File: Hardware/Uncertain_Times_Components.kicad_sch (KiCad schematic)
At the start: 73 parts, among them J1 Conn_01x12_Male, J2 Conn_01x16_Male, J3 Conn_01x14_Male, J4 Conn_01x12_Male, J5 SWD_Header, J6 Eurorack_10_pin_power, Q1 MMBT3904, Q2 MMBT3904, U1 LM1117-3.3, U2 STM32G473V, U3 LM1117-5.0, U4 TL074, U6 TL074, Y1 8MHz 20pF

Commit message: Schematic Updates
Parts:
- removed J6: Eurorack_10_pin_power, Custom_Footprints:Eurorack_10_pin_header, symbol Eurorack Header:Eurorack_10_pin_power
- added J7: Eurorack_16_pin_power, Custom_Footprints:Eurorack_16_pin_header, symbol Eurorack Header:Eurorack_16_pin_power
- added R1, R11, R12, R20, R24, R25: 560, Resistor_SMD:R_0603_1608Metric, symbol Device:R
- added R26: 15k, Resistor_SMD:R_0603_1608Metric, symbol Device:R_Small
- added R27: 10k, Resistor_SMD:R_0603_1608Metric, symbol Device:R_Small
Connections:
- net EnvA1_LED_Out is gone; now on net Sine3_Ramp_Lvl_LED: R80.1
- net EnvA2_LED_Out is gone; now on net Sine1_Swell_Lvl_LED: R81.1
- net EnvA3_LED_Out is gone; now on net Sine2_Swell_Lvl_LED: R82.1
- net EnvA4_LED_Out is gone; now on net Sine3_Swell_Lvl_LED: R83.1
- net EnvB1_LED_Out is gone; now on net Ramp_LED: R76.1
- net EnvB2_LED_Out is gone; now on net Swell_LED: R77.1
- net EnvB3_LED_Out is gone; now on net Sine1_Ramp_Lvl_LED: R78.1
- net EnvB4_LED_Out is gone; now on net Sine2_Ramp_Lvl_LED: R79.1
- net +12V_IN: now also J7.10 (Pin_10), J7.9 (Pin_9)
- net -12V_IN: now also J7.1 (Pin_1), J7.2 (Pin_2)
- net FM2_Out: now also J2.5 (Pin_5); no longer J2.7 (Pin_7)
- net FM3_Out: now also J2.6 (Pin_6); no longer J2.10 (Pin_10)
- net GND: now also J7.3 (Pin_3), J7.4 (Pin_4), J7.5 (Pin_5), J7.6 (Pin_6), J7.7 (Pin_7), J7.8 (Pin_8)
- net Sine1_DAC: now also R27.2
- net Sine1_Out: now also J2.2 (Pin_2)
- net Sine2_Out: now also J2.3 (Pin_3)
- net Sine3_Out: now also J2.4 (Pin_4)
- net Swell_Out: now also J2.7 (Pin_7); no longer J2.4 (Pin_4)
- net TIM2_CH3: now also R24.2
- net TIM2_CH4: now also R25.2
- net TIM4_CH1: now also R80.2
- net TIM4_CH2: now also R81.2
- net TIM4_CH3: now also R82.2
- net TIM4_CH4: now also R83.2
- net TIM8_CH1: now also R1.2
- net TIM8_CH2: now also R11.2
- net TIM8_CH3: now also R12.2
- net TIM8_CH4: now also R20.2
- net Sine1_Inv_Out: now reaches J2.8 (Pin_8)
- net Sine1_Inv_Out: now also U6.1, R26.1
- net Sine1_Ramp_Lvl_LED: now reaches J1.10 (Pin_10)
- net Sine2_Ramp_Rate_LED: now reaches J1.11 (Pin_11)
- net Sine2_Ramp_Rate_LED: now also R11.1
- net Sine2_Ramp_Lvl_LED: now reaches J1.12 (Pin_12)
- net Ramp_LED: now reaches J1.7 (Pin_7)
- net Swell_LED: now reaches J1.8 (Pin_8)
- net Sine1_Ramp_Rate_LED: now reaches J1.9 (Pin_9)
- net Sine1_Ramp_Rate_LED: now also R1.1
- net Gate_Normal: now reaches J3.1 (Pin_1)
- net Gate_Normal: now also J7.16 (Pin_16)
- net Sine3_Ramp_Rate_LED: now reaches J3.2 (Pin_2)
- net Sine3_Ramp_Rate_LED: now also R12.1
- net Sine3_Ramp_Lvl_LED: now reaches J3.3 (Pin_3)
- net Sine1_Swell_Rate_LED: now reaches J3.4 (Pin_4)
- net Sine1_Swell_Rate_LED: now also R20.1
- net Sine1_Swell_Lvl_LED: now reaches J3.5 (Pin_5)
- net Sine2_Swell_Rate_LED: now reaches J3.6 (Pin_6)
- net Sine2_Swell_Rate_LED: now also R24.1
- net Sine2_Swell_Lvl_LED: now reaches J3.7 (Pin_7)
- net Sine3_Swell_Rate_LED: now reaches J3.8 (Pin_8)
- net Sine3_Swell_Rate_LED: now also R25.1
- net Sine3_Swell_Lvl_LED: now reaches J3.9 (Pin_9)
- net at U6.2 (-): now also R26.2, R27.1; no longer U6.1
- no-connect marks 27 -> 31
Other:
- moved on the sheet: C21, C22, J3, U4E, U6A, U6E

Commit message: First draft of schematic
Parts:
- removed C17: 10uF, Capacitor_SMD:C_1206_3216Metric, symbol Device:C
- removed C20: 22uF, Capacitor_SMD:CP_Elec_4x5.8, symbol Device:C
- removed FID1: Fiducial, Custom_Footprints:4_Layer_Markers, symbol Mechanical:Fiducial
- removed J2: Conn_01x16_Male, Connector_PinHeader_2.54mm:PinHeader_1x16_P2.54mm_Vertical, symbol Connector:Conn_01x16_Male
- removed J3: Conn_01x14_Male, Connector_PinHeader_2.54mm:PinHeader_1x14_P2.54mm_Vertical, symbol Connector:Conn_01x14_Male
- removed TP6: TestPoint, Custom_Footprints:1mm_Test_Point, symbol Connector:TestPoint
- removed U1: LM1117-3.3, Package_TO_SOT_SMD:SOT-223-3_TabPin2, symbol Regulator_Linear:LM1117-3.3
- removed U3: LM1117-5.0, Package_TO_SOT_SMD:SOT-223-3_TabPin2, symbol Regulator_Linear:LM1117-5.0
- added J2: Conn_01x10_Male, Connector_PinHeader_2.54mm:PinHeader_1x10_P2.54mm_Vertical, symbol Connector:Conn_01x12_Pin
- added J3: Conn_01x12_Male, Connector_PinHeader_2.54mm:PinHeader_1x12_P2.54mm_Vertical, symbol Connector:Conn_01x16_Pin
- added J7: UART_Test_Pins, Custom_Footprints:SWD_header, symbol Connector:Conn_01x02_Pin
- added J8: USB_B_Micro, Custom_Footprints:USB_Micro-B_Amphenol, symbol Connector:USB_B_Micro
- added R34, R35, R36: 560, Resistor_SMD:R_0603_1608Metric, symbol Device:R
- added U2: STF202-22T1G, Custom_Footprints:STF202-22T1G, symbol STF202-22T1G:STF202-22T1G
- added U5: LT1117-3.3, Package_TO_SOT_SMD:SOT-223-3_TabPin2, symbol Regulator_Linear:LT1117-3.3
- C10: renamed from C11; symbol Encoder:CP_Small -> Device:C_Polarized_Small
- C11: renamed from C12; symbol Encoder:CP_Small -> Device:C_Polarized_Small
- C14: renamed from C6; symbol Encoder:CP_Small -> Device:C_Polarized_Small
- C17: renamed from C14; symbol Encoder:CP_Small -> Device:C_Polarized_Small
- J1: value Conn_01x12_Male -> Conn_01x10_Male; footprint Connector_PinHeader_2.54mm:PinHeader_1x12_P2.54mm_Vertical -> Connector_PinHeader_2.54mm:PinHeader_1x10_P2.54mm_Vertical; symbol Connector:Conn_01x12_Male -> Connector:Conn_01x12_Pin
- J4: symbol Connector:Conn_01x12_Male -> Connector:Conn_01x16_Pin
- J5: symbol Connector:Conn_01x04_Male -> Connector:Conn_01x04_Pin
- R14: renamed from R26; value 15k -> 20k
- R15: renamed from R21; value 15k -> 10k
- R16: renamed from R22; value 15k -> 10k
- R17: renamed from R23; value 15k -> 10k
- R6: renamed from R9; value 15k -> 10k
- R7: renamed from R10; value 15k -> 10k
- R8: renamed from R13; value 15k -> 10k
- R9: renamed from R14; value 15k -> 10k
- renumbered C2 to C1, C15 to C12, C16 to C13, C18 to C15, C19 to C16, C21 to C18, C22 to C19, C3 to C2, C4 to C3, C5 to C4, C7 to C5, C8 to C6, C9 to C7, C10 to C8, C13 to C9, D2 to D1, D3 to D2, J7 to J6, Q2 to Q1, Q1 to Q2, R2 to R1, R27 to R10, R15 to R11, R16 to R12, R17 to R13, R3 to R18, R18 to R19, R5 to R2, R76 to R20, R77 to R21, R78 to R22, R79 to R23, R80 to R24, R81 to R25, R82 to R26, R83 to R27, R1 to R28, R11 to R29, R6 to R3, R12 to R30, R20 to R31, R24 to R32, R25 to R33, R4 to R37, R19 to R38, R7 to R4, R8 to R5, U2 to U1, U4 to U3, U6 to U4
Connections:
- net +5V is gone; now on net +3.3V: TP3.1
- net +12V: now also U5.3 (VI)
- net +3.3V: now also J4.2 (Pin_2), J2.1 (Pin_1), U5.2 (VO); no longer TP4.1
- net +3.3VA: now also J4.5 (Pin_5), J2.9 (Pin_9); no longer J4.4 (Pin_4)
- net FM2_Out: now also J2.5 (Pin_5)
- net FM3_Out: now also J2.6 (Pin_6)
- net GND: now also J1.1 (Pin_1), J1.10 (Pin_10), J4.15 (Pin_15), J4.8 (Pin_8), TP4.1, J2.10 (Pin_10), J2.3 (Pin_3), J3.1 (Pin_1), J3.11 (Pin_11), J8.5 (GND), U2.6 (GND), U5.1 (GND); no longer J4.3 (Pin_3)
- net Gate_Normal: now also J6.15 (Pin_15), J3.2 (Pin_2)
- net Ramp_LED: now also J1.8 (Pin_8); no longer J1.7 (Pin_7)
- net Ramp_Level: now also J3.16 (Pin_16)
- net Ramp_Out: now also J3.12 (Pin_12)
- net Ramp_Rate: now also J3.15 (Pin_15)
- net Sine1_Inv_Out: now also J2.8 (Pin_8)
- net Sine1_Level: now also J1.11 (Pin_11)
- net Sine1_Lvl_Btn: now also J1.2 (Pin_2); no longer J1.1 (Pin_1)
- net Sine1_Out: now also J2.2 (Pin_2)
- net Sine1_Ramp_Lvl_LED: now also J4.10 (Pin_10), R25.1; no longer J1.10 (Pin_10), R22.1
- net Sine1_Ramp_Rate_LED: now also J4.9 (Pin_9), R31.1; no longer J1.9 (Pin_9), R28.1
- net Sine1_Rate: now also J2.12 (Pin_12)
- net Sine1_Rate_Btn: now also J1.5 (Pin_5); no longer J1.4 (Pin_4)
- net Sine1_Swell_Lvl_LED: now also R28.1, J3.6 (Pin_6); no longer R25.1
- net Sine1_Swell_Rate_LED: now also J3.5 (Pin_5), R34.1; no longer R31.1
- net Sine2_Level: now also J1.12 (Pin_12)
- net Sine2_Lvl_Btn: now also J1.3 (Pin_3); no longer J1.2 (Pin_2)
- net Sine2_Out: now also J4.3 (Pin_3)
- net Sine2_Ramp_Lvl_LED: now also J4.12 (Pin_12), R26.1; no longer J1.12 (Pin_12), R23.1
- net Sine2_Ramp_Rate_LED: now also J4.11 (Pin_11), R32.1; no longer J1.11 (Pin_11), R29.1
- net Sine2_Rate: now also J4.1 (Pin_1)
- net Sine2_Rate_Btn: now also J1.6 (Pin_6); no longer J1.5 (Pin_5)
- net Sine2_Swell_Lvl_LED: now also R29.1, J3.8 (Pin_8); no longer R26.1
- net Sine2_Swell_Rate_LED: now also J3.7 (Pin_7), R35.1; no longer R32.1
- net Sine3_Level: now also J2.11 (Pin_11)
- net Sine3_Lvl_Btn: now also J1.4 (Pin_4); no longer J1.3 (Pin_3)
- net Sine3_Out: now also J2.4 (Pin_4)
- net Sine3_Ramp_Lvl_LED: now also R27.1, J3.4 (Pin_4); no longer R24.1
- net Sine3_Ramp_Rate_LED: now also R33.1, J3.3 (Pin_3); no longer R30.1
- net Sine3_Rate: now also J3.13 (Pin_13)
- net Sine3_Rate_Btn: now also J1.7 (Pin_7); no longer J1.6 (Pin_6)
- net Sine3_Swell_Lvl_LED: now also R30.1, J3.10 (Pin_10); no longer R27.1
- net Sine3_Swell_Rate_LED: now also J3.9 (Pin_9), R36.1; no longer R33.1
- net Swell_LED: now also J1.9 (Pin_9); no longer J1.8 (Pin_8)
- net Swell_Level: now also J4.14 (Pin_14)
- net Swell_Out: now also J2.7 (Pin_7)
- net Swell_Rate: now also J4.13 (Pin_13)
- net TIM2_CH1: now also R32.2
- net TIM2_CH2: now also R33.2
- net TIM2_CH3: now also R34.2; no longer R32.2
- net TIM2_CH4: now also R35.2; no longer R33.2
- net USB_DM: now also U2.2 (D1_OUT); no longer J4.1 (Pin_1)
- net USB_DP: now also U2.3 (D2_OUT); no longer J4.2 (Pin_2)
- net Sine2_LED: now reaches J4.6 (Pin_6)
- net Sine2_LED: now also R23.1
- net Sine3_LED: now reaches J4.7 (Pin_7)
- net Sine3_LED: now also R24.1
- net USART1_TX: now reaches U1.30 (PC4)
- net USART1_TX: now also J7.1 (Pin_1)
- net USART1_RX: now reaches U1.31 (PC5)
- net USART1_RX: now also J7.2 (Pin_2)
- net Sine3_Swell_Rate: now reaches U1.9 (PC15)
- net Sine3_Swell_Rate: now also R36.2
- net CLK_IN renamed Clock_In
- net Clock_In: now also J3.14 (Pin_14)
- net GATE_IN renamed Gate_In
- net Gate_In: now also J4.16 (Pin_16)
- new net Sine1_LED: J4.4 (Pin_4), R22.1
- new net USB_D+: J8.3 (D+), U2.4 (D2_IN)
- new net USB_D-: J8.2 (D-), U2.5 (D1_IN)
- no-connect marks 31 -> 44
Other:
- note added: "Amplifiers"
- note added: "Connectors"
- note added: "Gain: 3.3 * (1 + 10k / 10k) = 6.6V Inverting: 3.3 * (20k / 10k) = -6.6V"
- note added: "Input Scaling"
- note added: "LED Resisitors"
- note removed: "Gain 2.5 output 8.25v"
- note removed: "LED resistors"
- note removed: "MIDI/SWD"
- note removed: "OpAmps"
- note removed: "Pitch Detection Multiplexer"
- moved on the sheet: C10, C11, C14, C17, C18, C19, D1, D2, J1, J5, J6, L1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

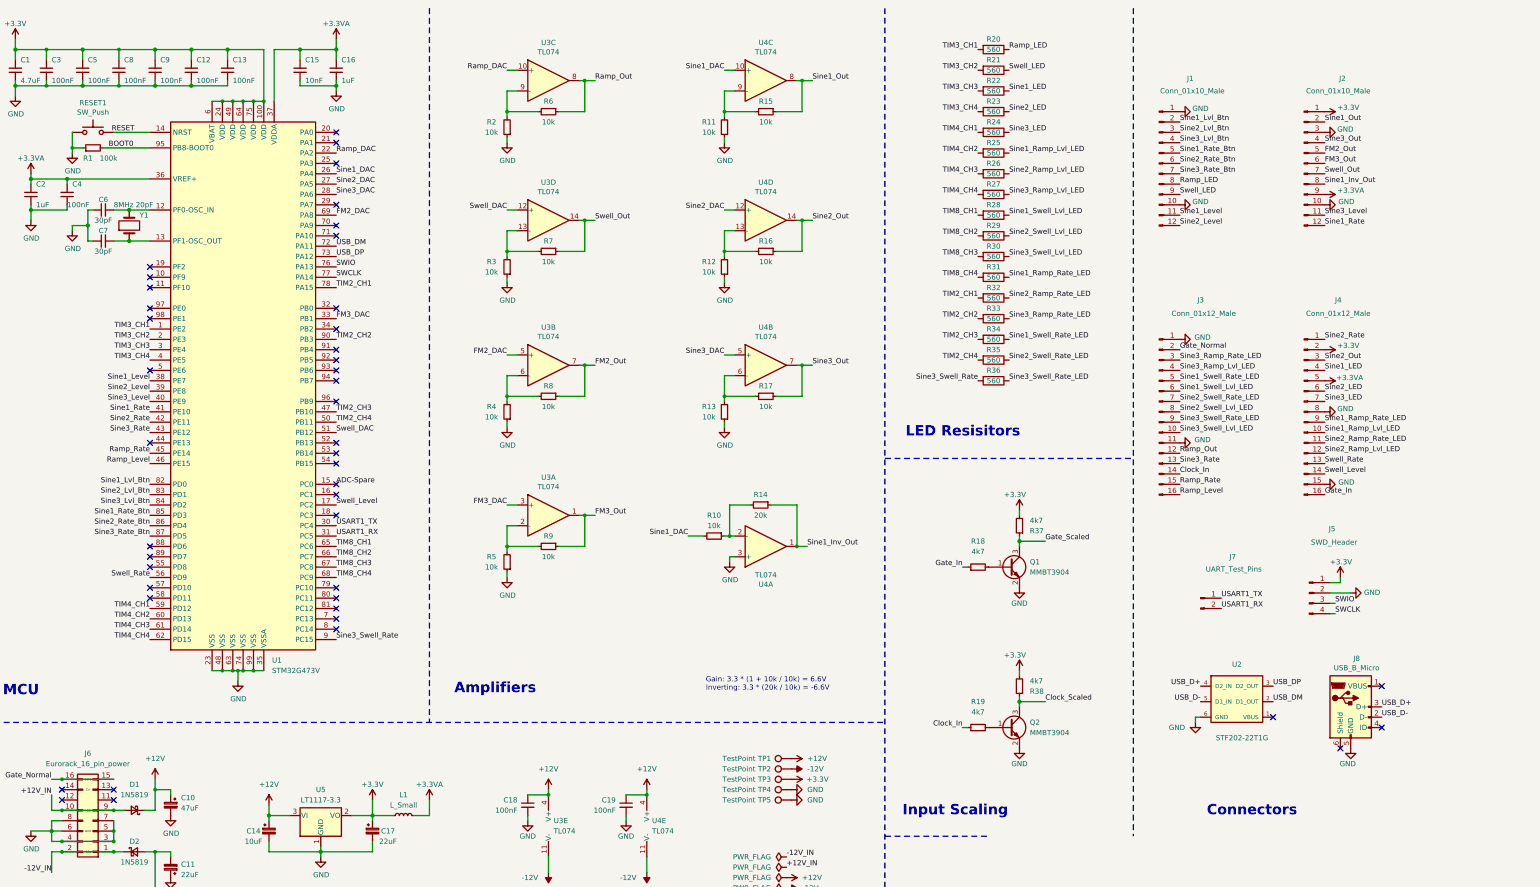
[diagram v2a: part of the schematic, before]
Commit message: Started routing components
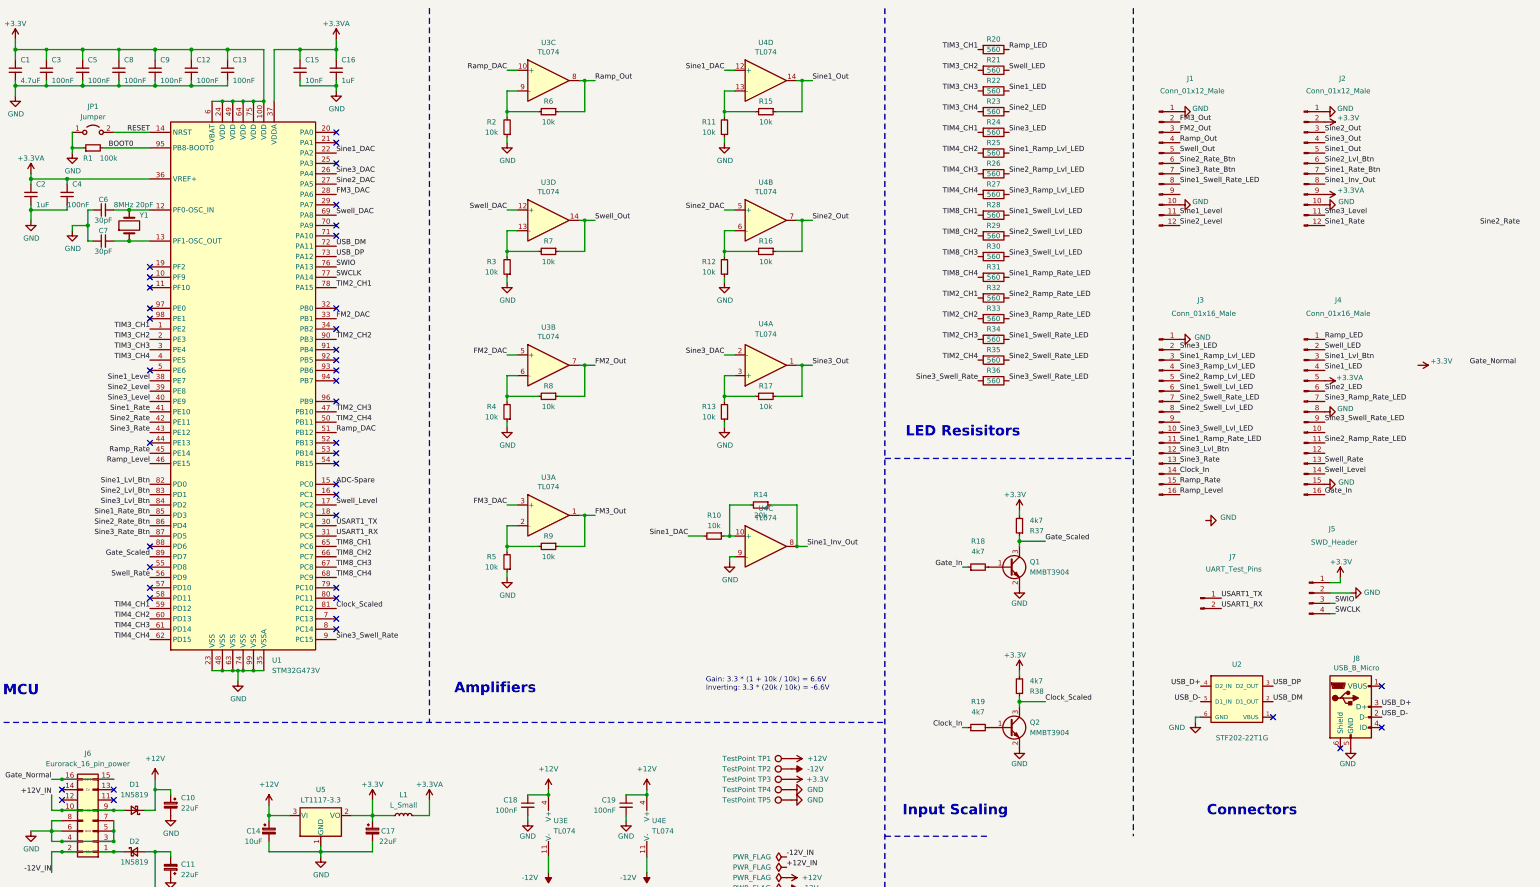
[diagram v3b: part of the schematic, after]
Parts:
- removed RESET1: SW_Push, Custom_Footprints:SW_SPST_EVQQ2, symbol Switch:SW_Push
- added JP1: Jumper, Jumper:SolderJumper-2_P1.3mm_Open_RoundedPad1.0x1.5mm, symbol Jumper:Jumper_2_Open
- C10: value 47uF -> 22uF
- J1, J2: value Conn_01x10_Male -> Conn_01x12_Male; footprint Connector_PinHeader_2.54mm:PinHeader_1x10_P2.54mm_Vertical -> Connector_PinHeader_2.54mm:PinHeader_1x12_P2.54mm_Vertical
- J3, J4: value Conn_01x12_Male -> Conn_01x16_Male; footprint Connector_PinHeader_2.54mm:PinHeader_1x12_P2.54mm_Vertical -> Connector_PinHeader_2.54mm:PinHeader_1x16_P2.54mm_Vertical
- J7: footprint Custom_Footprints:SWD_header -> Connector_PinHeader_2.54mm:PinHeader_1x02_P2.54mm_Vertical
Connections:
- net +3.3V: now also J2.2 (Pin_2); no longer J2.1 (Pin_1), J4.2 (Pin_2)
- net Clock_Scaled: now also U1.81 (PC12)
- net FM2_DAC: now also U1.33 (PB1); no longer U1.69 (PA8)
- net FM2_Out: now also J1.3 (Pin_3); no longer J2.5 (Pin_5)
- net FM3_DAC: now also U1.28 (PA6); no longer U1.33 (PB1)
- net FM3_Out: now also J1.2 (Pin_2); no longer J2.6 (Pin_6)
- net GND: now also J2.1 (Pin_1), U4.9 (-), JP1.1 (A); no longer J2.3 (Pin_3), J3.11 (Pin_11), U4.3 (+)
- net Gate_Normal: no longer J3.2 (Pin_2)
- net Gate_Scaled: now also U1.89 (PD7)
- net RESET: now also JP1.2 (B)
- net Ramp_DAC: now also U1.51 (PB12); no longer U1.22 (PA2)
- net Ramp_LED: now also J4.1 (Pin_1); no longer J1.8 (Pin_8)
- net Ramp_Out: now also J1.4 (Pin_4); no longer J3.12 (Pin_12)
- net Sine1_DAC: now also U1.22 (PA2), U4.12 (+); no longer U1.26 (PA4), U4.10 (+)
- net Sine1_Inv_Out: now also U4.8; no longer U4.1
- net Sine1_Lvl_Btn: now also J4.3 (Pin_3); no longer J1.2 (Pin_2)
- net Sine1_Out: now also J2.5 (Pin_5), U4.14; no longer J2.2 (Pin_2), U4.8
- net Sine1_Ramp_Lvl_LED: now also J3.3 (Pin_3); no longer J4.10 (Pin_10)
- net Sine1_Ramp_Rate_LED: now also J3.11 (Pin_11); no longer J4.9 (Pin_9)
- net Sine1_Rate_Btn: now also J2.7 (Pin_7); no longer J1.5 (Pin_5)
- net Sine1_Swell_Rate_LED: now also J1.8 (Pin_8); no longer J3.5 (Pin_5)
- net Sine2_DAC: now also U4.5 (+); no longer U4.12 (+)
- net Sine2_Lvl_Btn: now also J2.6 (Pin_6); no longer J1.3 (Pin_3)
- net Sine2_Out: now also J2.3 (Pin_3), U4.7; no longer J4.3 (Pin_3), U4.14
- net Sine2_Ramp_Lvl_LED: now also J3.5 (Pin_5); no longer J4.12 (Pin_12)
- net Sine2_Rate: no longer J4.1 (Pin_1)
- net Sine3_DAC: now also U1.26 (PA4), U4.2 (-); no longer U1.28 (PA6), U4.5 (+)
- net Sine3_LED: now also J3.2 (Pin_2); no longer J4.7 (Pin_7)
- net Sine3_Lvl_Btn: now also J3.12 (Pin_12); no longer J1.4 (Pin_4)
- net Sine3_Out: now also U4.1; no longer U4.7
- net Sine3_Ramp_Rate_LED: now also J4.7 (Pin_7); no longer J3.3 (Pin_3)
- net Sine3_Swell_Rate_LED: now also J4.9 (Pin_9); no longer J3.9 (Pin_9)
- net Swell_DAC: now also U1.69 (PA8); no longer U1.51 (PB12)
- net Swell_LED: now also J4.2 (Pin_2); no longer J1.9 (Pin_9)
- net Swell_Out: now also J1.5 (Pin_5); no longer J2.7 (Pin_7)
- net at R11.2, R15.2: now also U4.13 (-); no longer U4.9 (-)
- net at R13.2, R17.2: now also U4.3 (+); no longer U4.6 (-)
- net at R12.2, R16.2: now also U4.6 (-); no longer U4.13 (-)
- net at R10.1, R14.2: now also U4.10 (+); no longer U4.2 (-)
- no-connect marks 44 -> 42
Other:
- moved on the sheet: U4A, U4B, U4C, U4D

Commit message: Update Uncertain_Times_Components.kicad_sch
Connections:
- net +3.3VA: no longer J4.5 (Pin_5)
- net GND: now also J4.9 (Pin_9); no longer J4.8 (Pin_8)
- net Ramp_LED: now also J4.5 (Pin_5); no longer J4.1 (Pin_1)
- net Sine1_LED: now also J4.3 (Pin_3); no longer J4.4 (Pin_4)
- net Sine1_Level: now also U1.40 (PE9); no longer U1.38 (PE7)
- net Sine1_Lvl_Btn: no longer J4.3 (Pin_3)
- net Sine1_Rate: now also U1.39 (PE8); no longer U1.41 (PE10)
- net Sine2_LED: now also J4.2 (Pin_2); no longer J4.6 (Pin_6)
- net Sine2_Level: now also U1.41 (PE10); no longer U1.39 (PE8)
- net Sine2_Ramp_Lvl_LED: now also J3.4 (Pin_4); no longer J3.5 (Pin_5)
- net Sine3_LED: now also J4.6 (Pin_6); no longer J3.2 (Pin_2)
- net Sine3_Level: now also U1.38 (PE7); no longer U1.40 (PE9)
- net Sine3_Ramp_Lvl_LED: now also J3.5 (Pin_5); no longer J3.4 (Pin_4)
- net Sine3_Ramp_Rate_LED: now also J3.2 (Pin_2); no longer J4.7 (Pin_7)
- net Sine3_Swell_Rate_LED: now also J4.1 (Pin_1); no longer J4.9 (Pin_9)
- net Swell_LED: now also J4.4 (Pin_4); no longer J4.2 (Pin_2)
- net TIM2_CH2: now also R24.2; no longer R33.2
- net TIM4_CH1: now also R33.2; no longer R24.2
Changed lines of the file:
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@@
 	)
 	(label "Sine2_LED"
-		(at 341.63 106.68 0)
+		(at 341.63 96.52 0)
 		(fields_autoplaced yes)
 		(effects
@@
 	)
 	(label "Ramp_LED"
-		(at 341.63 93.98 0)
+		(at 341.63 104.14 0)
 		(fields_autoplaced yes)
 		(effects
@@
 	)
 	(label "TIM4_CH1"
-		(at 256.54 43.18 180)
+		(at 256.54 88.9 180)
 		(fields_autoplaced yes)
 		(effects
@@
 	)
 	(label "Sine3_Ramp_Lvl_LED"
-		(at 306.07 101.6 0)
+		(at 306.07 104.14 0)
 		(fields_autoplaced yes)
 		(effects
@@
 	)
 	(label "Sine1_Rate"
-		(at 53.34 111.76 180)
+		(at 53.34 106.68 180)
 		(fields_autoplaced yes)
 		(effects
@@
 	)
 	(label "Sine2_Ramp_Lvl_LED"
-		(at 306.07 104.14 0)
+		(at 306.07 101.6 0)
 		(fields_autoplaced yes)
 		(effects
@@
 	)
 	(label "Sine2_Level"
-		(at 53.34 106.68 180)
+		(at 53.34 111.76 180)
 		(fields_autoplaced yes)
 		(effects
@@
 	)
 	(label "Sine3_Level"
-		(at 53.34 109.22 180)
+		(at 53.34 104.14 180)
 		(fields_autoplaced yes)
 		(effects
@@
 	)
 	(label "Sine3_Ramp_Rate_LED"
-		(at 341.63 109.22 0)
+		(at 306.07 96.52 0)
 		(fields_autoplaced yes)
 		(effects
@@
 	)
 	(label "Sine3_LED"
-		(at 306.07 96.52 0)
+		(at 341.63 106.68 0)
 		(fields_autoplaced yes)
 		(effects
@@
 	)
 	(label "Sine1_LED"
-		(at 341.63 101.6 0)
+		(at 341.63 99.06 0)
 		(fields_autoplaced yes)
 		(effects
@@
 	)
 	(label "Sine1_Lvl_Btn"
-		(at 341.63 99.06 0)
+		(at 382.27 106.68 0)
 		(fields_autoplaced yes)
 		(effects
@@
 	)
 	(label "Sine3_Swell_Rate_LED"
-		(at 341.63 114.3 0)
+		(at 341.63 93.98 0)
 		(fields_autoplaced yes)
 		(effects
@@
 	)
 	(label "Swell_LED"
-		(at 341.63 96.52 0)
+		(at 341.63 101.6 0)
 		(fields_autoplaced yes)
 		(effects
@@
 	)
 	(label "TIM2_CH2"
-		(at 256.54 88.9 180)
+		(at 256.54 43.18 180)
 		(fields_autoplaced yes)
 		(effects
@@
 	)
 	(label "Sine1_Level"
-		(at 53.34 104.14 180)
+		(at 53.34 109.22 180)
 		(fields_autoplaced yes)
 		(effects
@@
 	(symbol
 		(lib_id "power:+3.3VA")
-		(at 341.63 104.14 270)
+		(at 363.22 110.49 270)
 		(unit 1)
 		(exclude_from_sim no)
@@
 		(dnp no)
 		(property "Reference" "#PWR04"
-			(at 337.82 104.14 0)
+			(at 359.41 110.49 0)
 			(effects
 				(font
@@
 		)
 		(property "Value" "+3.3VA"
-			(at 344.424 103.378 90)
+			(at 366.014 109.728 90)
 			(effects
 				(font
@@
 		)
 		(property "Footprint" ""
-			(at 341.63 104.14 0)
+			(at 363.22 110.49 0)
 			(effects
 				(font
@@
 		)
 		(property "Datasheet" ""
-			(at 341.63 104.14 0)
+			(at 363.22 110.49 0)
 			(effects
 				(font
@@
 		)
 		(property "Description" "Power symbol creates a global label with name \"+3.3VA\""
-			(at 341.63 104.14 0)
+			(at 363.22 110.49 0)
 			(effects
 				(font
@@
 	(symbol
 		(lib_id "power:GND")
-		(at 341.63 111.76 90)
+		(at 341.63 114.3 90)
 		(unit 1)
 		(exclude_from_sim no)
@@
 		(dnp no)
 		(property "Reference" "#PWR033"
-			(at 347.98 111.76 0)
+			(at 347.98 114.3 0)
 			(effects
 				(font
@@
 		)
 		(property "Value" "GND"
-			(at 344.678 110.998 90)
+			(at 344.678 113.538 90)
 			(effects
 				(font
@@
 		)
 		(property "Footprint" ""
-			(at 341.63 111.76 0)
+			(at 341.63 114.3 0)
 			(effects
 				(font
@@
 		)
 		(property "Datasheet" ""
-			(at 341.63 111.76 0)
+			(at 341.63 114.3 0)
 			(effects
 				(font
@@
 		)
 		(property "Description" "Power symbol creates a global label with name \"GND\" , ground"
-			(at 341.63 111.76 0)
+			(at 341.63 114.3 0)
 			(effects
 				(font
